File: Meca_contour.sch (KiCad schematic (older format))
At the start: 4 parts

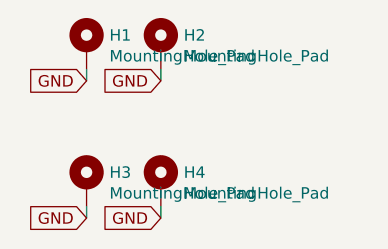
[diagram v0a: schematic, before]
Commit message: schema + routage
- redistribution des touches
- ajout 5ways switch
- supprimé les empreintes pcb de touches résistives
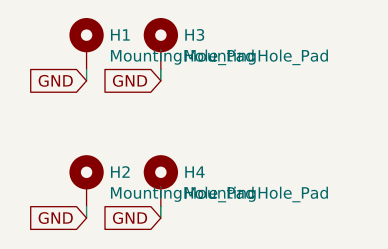
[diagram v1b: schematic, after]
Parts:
- renumbered H3 to H2, H2 to H3
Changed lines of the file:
@@
 	1000 1150 1000 1200
 $Comp
-L Mechanical:MountingHole_Pad H3
+L Mechanical:MountingHole_Pad H2
 U 1 1 5FCCD464
 P 1000 1650
-F 0 "H3" H 1100 1699 50  0000 L CNN
+F 0 "H2" H 1100 1699 50  0000 L CNN
 F 1 "MountingHole_Pad" H 1100 1608 50  0000 L CNN
 F 2 "MountingHole:MountingHole_3.2mm_M3_Pad_Via" H 1000 1650 50  0001 C CNN
@@
 	1000 1750 1000 1800
 $Comp
-L Mechanical:MountingHole_Pad H2
+L Mechanical:MountingHole_Pad H3
 U 1 1 5FCD7741
 P 1325 1050
-F 0 "H2" H 1425 1099 50  0000 L CNN
+F 0 "H3" H 1425 1099 50  0000 L CNN
 F 1 "MountingHole_Pad" H 1425 1008 50  0000 L CNN
 F 2 "MountingHole:MountingHole_3.2mm_M3_Pad_Via" H 1325 1050 50  0001 C CNN
